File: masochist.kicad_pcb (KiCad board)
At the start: 2 copper layers, 195.3 x 103.2 mm, 76 parts, among them J1 USB_C_Receptacle_USB2.0, J2 AVR-ISP-6, SW1 RESET, SW2 SW_Push, U1 ATmega328P-PU, Y1 Crystal

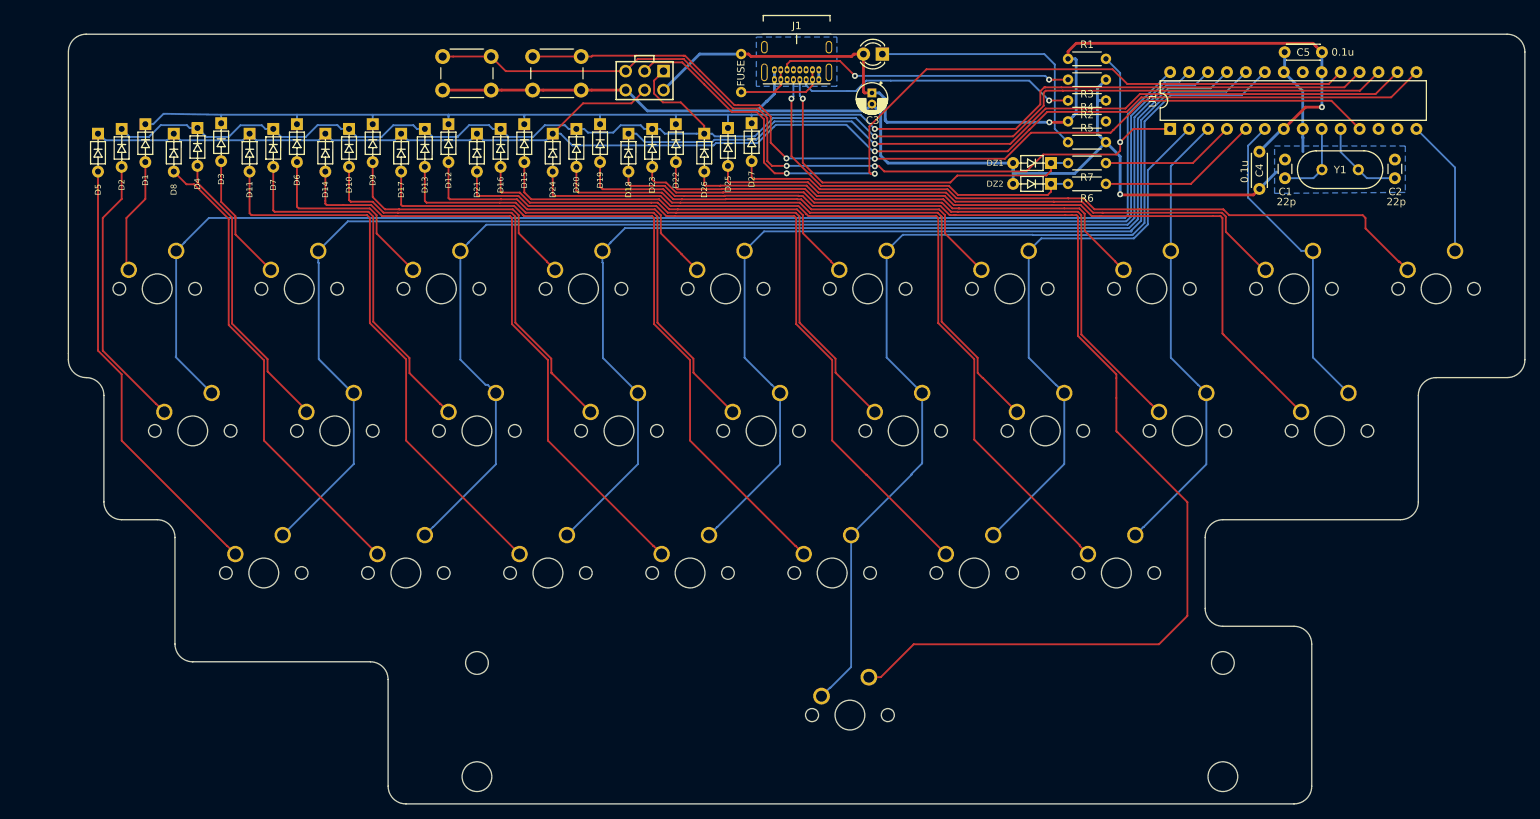
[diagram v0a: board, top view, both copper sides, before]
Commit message: added some mounting holes, waiting for feedback
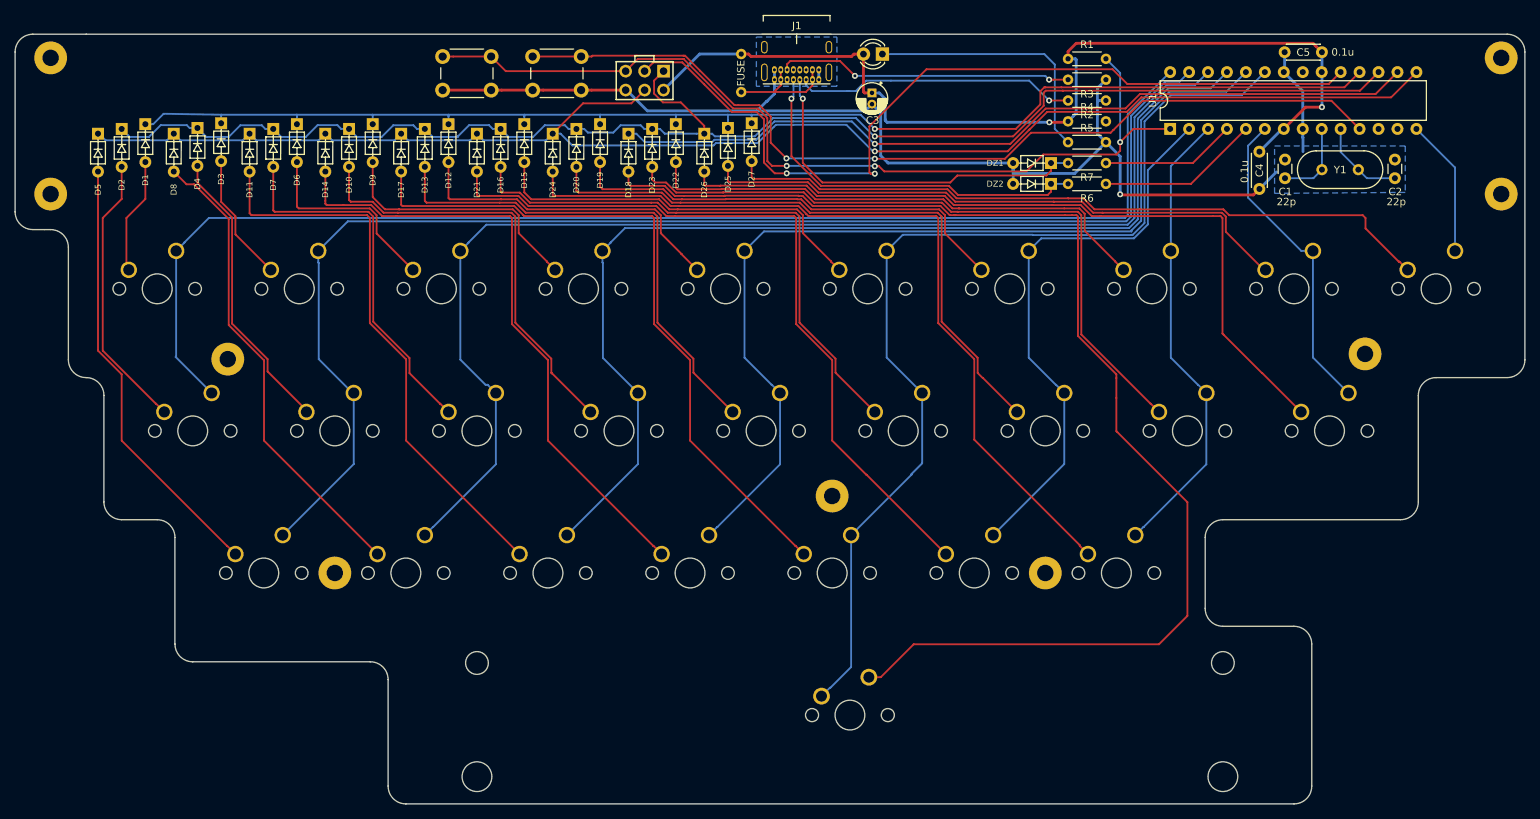
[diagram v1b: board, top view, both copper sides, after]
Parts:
- added REF**: MountingHole_2.2mm_M2_Pad, cftkb:MountingHole_2.2mm_M2_Pad, F.Cu at (63.5, 53.2)
- added REF**: MountingHole_2.2mm_M2_Pad, cftkb:MountingHole_2.2mm_M2_Pad, F.Cu at (63.5, 34.9)
- added REF**: MountingHole_2.2mm_M2_Pad, cftkb:MountingHole_2.2mm_M2_Pad, F.Cu at (258.0, 53.2)
- added REF**: MountingHole_2.2mm_M2_Pad, cftkb:MountingHole_2.2mm_M2_Pad, F.Cu at (258.0, 34.9)
- added REF**: MountingHole_2.2mm_M2_Pad, cftkb:MountingHole_2.2mm_M2_Pad, F.Cu at (168.3, 93.7)
- added REF**: MountingHole_2.2mm_M2_Pad, cftkb:MountingHole_2.2mm_M2_Pad, F.Cu at (239.7, 74.6)
- added REF**: MountingHole_2.2mm_M2_Pad, cftkb:MountingHole_2.2mm_M2_Pad, F.Cu at (196.8, 104.0)
- added REF**: MountingHole_2.2mm_M2_Pad, cftkb:MountingHole_2.2mm_M2_Pad, F.Cu at (101.6, 104.0)
- added REF**: MountingHole_2.2mm_M2_Pad, cftkb:MountingHole_2.2mm_M2_Pad, F.Cu at (87.2, 75.3)
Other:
- board size 195.3 x 103.2 mm -> 202.4 x 103.2 mm
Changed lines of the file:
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@@
   (general
     (thickness 1.6)
-    (drawings 32)
+    (drawings 37)
     (tracks 913)
     (zones 0)
-    (modules 76)
+    (modules 85)
     (nets 62)
   )
@@
     (add_net GND)
   )
+  (module cftkb:MountingHole_2.2mm_M2_Pad (layer F.Cu)
+    (at 63.5 53.18125)
+    (descr "Mounting Hole 2.2mm, M2")
+    (tags "mounting hole 2.2mm m2")
+    (attr virtual)
+    (fp_text reference REF** (at 0 -3.2) (layer Cmts.User)
+      (effects (font (size 1 1) (thickness 0.15)))
+    )
+    (fp_text value MountingHole_2.2mm_M2_Pad (at 0 3.2) (layer F.Fab)
+      (effects (font (size 1 1) (thickness 0.15)))
+    )
+    (fp_circle (center 0 0) (end 2.45 0) (layer F.CrtYd) (width 0.05))
+    (fp_circle (center 0 0) (end 2.2 0) (layer Cmts.User) (width 0.15))
+    (fp_text user %R (at 0.3 0) (layer F.Fab)
+      (effects (font (size 1 1) (thickness 0.15)))
+    )
+    (pad 1 thru_hole circle (at 0 0) (size 4.4 4.4) (drill 2.2) (layers *.Cu *.Mask))
+  )
+  (module cftkb:MountingHole_2.2mm_M2_Pad (layer F.Cu)
+    (at 63.5 34.925)
+    (descr "Mounting Hole 2.2mm, M2")
+    (tags "mounting hole 2.2mm m2")
+    (attr virtual)
+    (fp_text reference REF** (at 0 -3.2) (layer Cmts.User)
+      (effects (font (size 1 1) (thickness 0.15)))
+    )
+    (fp_text value MountingHole_2.2mm_M2_Pad (at 0 3.2) (layer F.Fab)
+      (effects (font (size 1 1) (thickness 0.15)))
+    )
+    (fp_circle (center 0 0) (end 2.45 0) (layer F.CrtYd) (width 0.05))
+    (fp_circle (center 0 0) (end 2.2 0) (layer Cmts.User) (width 0.15))
+    (fp_text user %R (at 0.3 0) (layer F.Fab)
+      (effects (font (size 1 1) (thickness 0.15)))
+    )
+    (pad 1 thru_hole circle (at 0 0) (size 4.4 4.4) (drill 2.2) (layers *.Cu *.Mask))
+  )
+  (module cftkb:MountingHole_2.2mm_M2_Pad (layer F.Cu)
+    (at 257.96875 53.18125)
+    (descr "Mounting Hole 2.2mm, M2")
+    (tags "mounting hole 2.2mm m2")
+    (attr virtual)
+    (fp_text reference REF** (at 0 -3.2) (layer Cmts.User)
+      (effects (font (size 1 1) (thickness 0.15)))
+    )
+    (fp_text value MountingHole_2.2mm_M2_Pad (at 0 3.2) (layer F.Fab)
+      (effects (font (size 1 1) (thickness 0.15)))
+    )
+    (fp_circle (center 0 0) (end 2.45 0) (layer F.CrtYd) (width 0.05))
+    (fp_circle (center 0 0) (end 2.2 0) (layer Cmts.User) (width 0.15))
+    (fp_text user %R (at 0.3 0) (layer F.Fab)
+      (effects (font (size 1 1) (thickness 0.15)))
+    )
+    (pad 1 thru_hole circle (at 0 0) (size 4.4 4.4) (drill 2.2) (layers *.Cu *.Mask))
+  )
+  (module cftkb:MountingHole_2.2mm_M2_Pad (layer F.Cu)
+    (at 257.96875 34.925)
+    (descr "Mounting Hole 2.2mm, M2")
+    (tags "mounting hole 2.2mm m2")
+    (attr virtual)
+    (fp_text reference REF** (at 0 -3.2) (layer Cmts.User)
+      (effects (font (size 1 1) (thickness 0.15)))
+    )
+    (fp_text value MountingHole_2.2mm_M2_Pad (at 0 3.2) (layer F.Fab)
+      (effects (font (size 1 1) (thickness 0.15)))
+    )
+    (fp_circle (center 0 0) (end 2.45 0) (layer F.CrtYd) (width 0.05))
+    (fp_circle (center 0 0) (end 2.2 0) (layer Cmts.User) (width 0.15))
+    (fp_text user %R (at 0.3 0) (layer F.Fab)
+      (effects (font (size 1 1) (thickness 0.15)))
+    )
+    (pad 1 thru_hole circle (at 0 0) (size 4.4 4.4) (drill 2.2) (layers *.Cu *.Mask))
+  )
+  (module cftkb:MountingHole_2.2mm_M2_Pad (layer F.Cu)
+    (at 168.275 93.6625)
+    (descr "Mounting Hole 2.2mm, M2")
+    (tags "mounting hole 2.2mm m2")
+    (attr virtual)
+    (fp_text reference REF** (at 0 -3.2) (layer Cmts.User)
+      (effects (font (size 1 1) (thickness 0.15)))
+    )
+    (fp_text value MountingHole_2.2mm_M2_Pad (at 0 3.2) (layer F.Fab)
+      (effects (font (size 1 1) (thickness 0.15)))
+    )
+    (fp_circle (center 0 0) (end 2.45 0) (layer F.CrtYd) (width 0.05))
+    (fp_circle (center 0 0) (end 2.2 0) (layer Cmts.User) (width 0.15))
+    (fp_text user %R (at 0.3 0) (layer F.Fab)
+      (effects (font (size 1 1) (thickness 0.15)))
+    )
+    (pad 1 thru_hole circle (at 0 0) (size 4.4 4.4) (drill 2.2) (layers *.Cu *.Mask))
+  )
+  (module cftkb:MountingHole_2.2mm_M2_Pad (layer F.Cu)
+    (at 239.7125 74.6125)
+    (descr "Mounting Hole 2.2mm, M2")
+    (tags "mounting hole 2.2mm m2")
+    (attr virtual)
+    (fp_text reference REF** (at 0 -3.2) (layer Cmts.User)
+      (effects (font (size 1 1) (thickness 0.15)))
+    )
+    (fp_text value MountingHole_2.2mm_M2_Pad (at 0 3.2) (layer F.Fab)
+      (effects (font (size 1 1) (thickness 0.15)))
+    )
+    (fp_circle (center 0 0) (end 2.45 0) (layer F.CrtYd) (width 0.05))
+    (fp_circle (center 0 0) (end 2.2 0) (layer Cmts.User) (width 0.15))
+    (fp_text user %R (at 0.3 0) (layer F.Fab)
+      (effects (font (size 1 1) (thickness 0.15)))
+    )
+    (pad 1 thru_hole circle (at 0 0) (size 4.4 4.4) (drill 2.2) (layers *.Cu *.Mask))
+  )
+  (module cftkb:MountingHole_2.2mm_M2_Pad (layer F.Cu)
+    (at 196.85 103.98125)
+    (descr "Mounting Hole 2.2mm, M2")
+    (tags "mounting hole 2.2mm m2")
+    (attr virtual)
+    (fp_text reference REF** (at 0 -3.2) (layer Cmts.User)
+      (effects (font (size 1 1) (thickness 0.15)))
+    )
+    (fp_text value MountingHole_2.2mm_M2_Pad (at 0 3.2) (layer F.Fab)
+      (effects (font (size 1 1) (thickness 0.15)))
+    )
+    (fp_circle (center 0 0) (end 2.45 0) (layer F.CrtYd) (width 0.05))
+    (fp_circle (center 0 0) (end 2.2 0) (layer Cmts.User) (width 0.15))
+    (fp_text user %R (at 0.3 0) (layer F.Fab)
+      (effects (font (size 1 1) (thickness 0.15)))
+    )
+    (pad 1 thru_hole circle (at 0 0) (size 4.4 4.4) (drill 2.2) (layers *.Cu *.Mask))
+  )
+  (module cftkb:MountingHole_2.2mm_M2_Pad (layer F.Cu)
+    (at 101.6 103.98125)
+    (descr "Mounting Hole 2.2mm, M2")
+    (tags "mounting hole 2.2mm m2")
+    (attr virtual)
+    (fp_text reference REF** (at 0 -3.2) (layer Cmts.User)
+      (effects (font (size 1 1) (thickness 0.15)))
+    )
+    (fp_text value MountingHole_2.2mm_M2_Pad (at 0 3.2) (layer F.Fab)
+      (effects (font (size 1 1) (thickness 0.15)))
+    )
+    (fp_circle (center 0 0) (end 2.45 0) (layer F.CrtYd) (width 0.05))
+    (fp_circle (center 0 0) (end 2.2 0) (layer Cmts.User) (width 0.15))
+    (fp_text user %R (at 0.3 0) (layer F.Fab)
+      (effects (font (size 1 1) (thickness 0.15)))
+    )
+    (pad 1 thru_hole circle (at 0 0) (size 4.4 4.4) (drill 2.2) (layers *.Cu *.Mask))
+  )
+  (module cftkb:MountingHole_2.2mm_M2_Pad (layer F.Cu)
+    (at 87.249 75.311)
+    (descr "Mounting Hole 2.2mm, M2")
+    (tags "mounting hole 2.2mm m2")
+    (attr virtual)
+    (fp_text reference REF** (at 0 -3.2) (layer Cmts.User)
+      (effects (font (size 1 1) (thickness 0.15)))
+    )
+    (fp_text value MountingHole_2.2mm_M2_Pad (at 0 3.2) (layer F.Fab)
+      (effects (font (size 1 1) (thickness 0.15)))
+    )
+    (fp_circle (center 0 0) (end 2.45 0) (layer F.CrtYd) (width 0.05))
+    (fp_circle (center 0 0) (end 2.2 0) (layer Cmts.User) (width 0.15))
+    (fp_text user %R (at 0.3 0) (layer F.Fab)
+      (effects (font (size 1 1) (thickness 0.15)))
+    )
+    (pad 1 thru_hole circle (at 0 0) (size 4.4 4.4) (drill 2.2) (layers *.Cu *.Mask))
+  )
   (module cftkb:Crystal_HC49-4H_Vertical (layer F.Cu)
     (at 233.934 49.911)
@@
     )
   )
+  (gr_line (start 62.70625 57.94375) (end 63.5 57.94375) (layer Edge.Cuts) (width 0.05))
+  (gr_line (start 61.11875 57.94375) (end 62.70625 57.94375) (layer Edge.Cuts) (width 0.05))
+  (gr_line (start 58.7375 34.13125) (end 58.7375 55.5625) (layer Edge.Cuts) (width 0.05))
+  (gr_arc (start 61.11875 55.5625) (end 58.7375 55.5625) (angle -90) (layer Edge.Cuts) (width 0.05))
+  (gr_line (start 65.88125 75.40625) (end 65.88125 60.325) (layer Edge.Cuts) (width 0.05))
+  (gr_arc (start 63.5 60.325) (end 65.88125 60.325) (angle -90) (layer Edge.Cuts) (width 0.05))
+  (gr_arc (start 68.2625 75.40625) (end 65.88125 75.40625) (angle -90) (layer Edge.Cuts) (width 0.05))
+  (gr_line (start 68.2625 31.75) (end 61.11875 31.75) (layer Edge.Cuts) (width 0.05))
+  (gr_arc (start 61.11875 34.13125) (end 61.11875 31.75) (angle -90) (layer Edge.Cuts) (width 0.05))
   (gr_line (start 261.14375 75.40625) (end 261.14375 34.13125) (layer Edge.Cuts) (width 0.05))
   (gr_line (start 249.2375 77.7875) (end 258.7625 77.7875) (layer Edge.Cuts) (width 0.05))
@@
   (gr_arc (start 73.025 94.45625) (end 70.64375 94.45625) (angle -90) (layer Edge.Cuts) (width 0.05))
   (gr_arc (start 68.2625 80.16875) (end 70.64375 80.16875) (angle -90) (layer Edge.Cuts) (width 0.05))
-  (gr_line (start 65.88125 74.6125) (end 65.88125 75.40625) (layer Edge.Cuts) (width 0.05))
-  (gr_arc (start 68.2625 75.40625) (end 65.88125 75.40625) (angle -90) (layer Edge.Cuts) (width 0.05))
-  (gr_line (start 65.88125 34.13125) (end 65.88125 74.6125) (layer Edge.Cuts) (width 0.05))
   (gr_line (start 258.7625 31.75) (end 68.2625 31.75) (layer Edge.Cuts) (width 0.05))
   (gr_arc (start 258.7625 34.13125) (end 261.14375 34.13125) (angle -90) (layer Edge.Cuts) (width 0.05))
-  (gr_arc (start 68.2625 34.13125) (end 68.2625 31.75) (angle -90) (layer Edge.Cuts) (width 0.05))
   (segment (start 228.82225 34.27475) (end 228.934 34.163) (width 0.25) (layer B.Cu) (net 1))
   (segment (start 231.36225 44.45) (end 231.394 44.45) (width 0.25) (layer F.Cu) (net 1))

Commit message: passes DRC, all traces connected
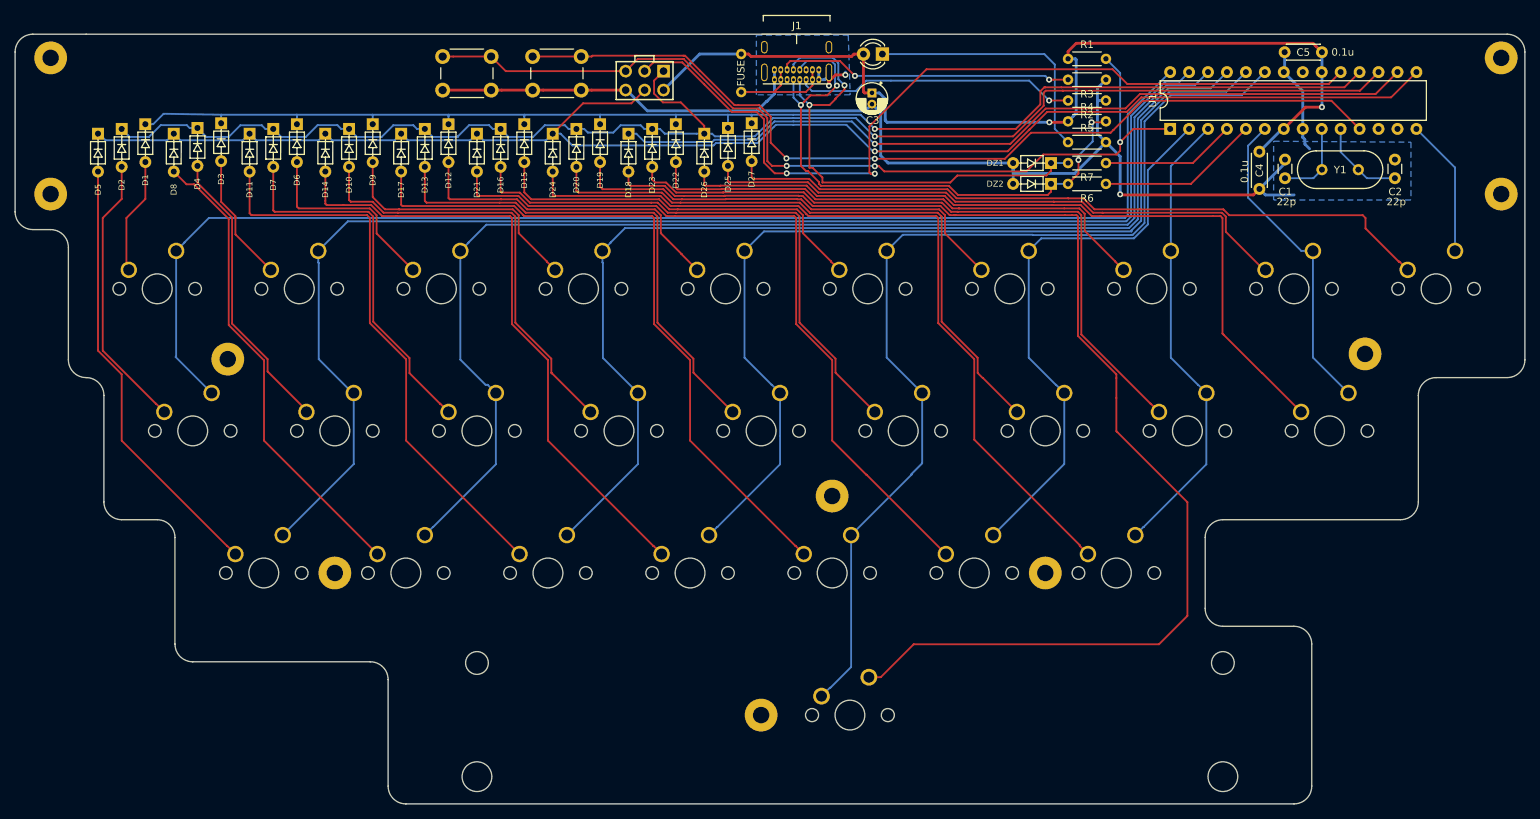
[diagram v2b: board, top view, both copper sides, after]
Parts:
- added REF**: MountingHole_2.2mm_M2_Pad, cftkb:MountingHole_2.2mm_M2_Pad, F.Cu at (158.8, 123.0)
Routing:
- net Net-(DZ2-Pad1): track 50.9 -> 77.0 mm, vias 1 -> 4
- net Net-(DZ1-Pad1): track 49.7 -> 66.9 mm, vias 1 -> 2
- net GND: track 166.5 -> 180.9 mm, vias 1 -> 3
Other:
- board text added: "Designed by Reid"
- board text added: "Masochist"

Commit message: added some cool dude's face to the silkscreen B)
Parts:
- added G***: LOGO, silkscreen:reid_face_tiny, B.Cu at (212.3, 120.9)

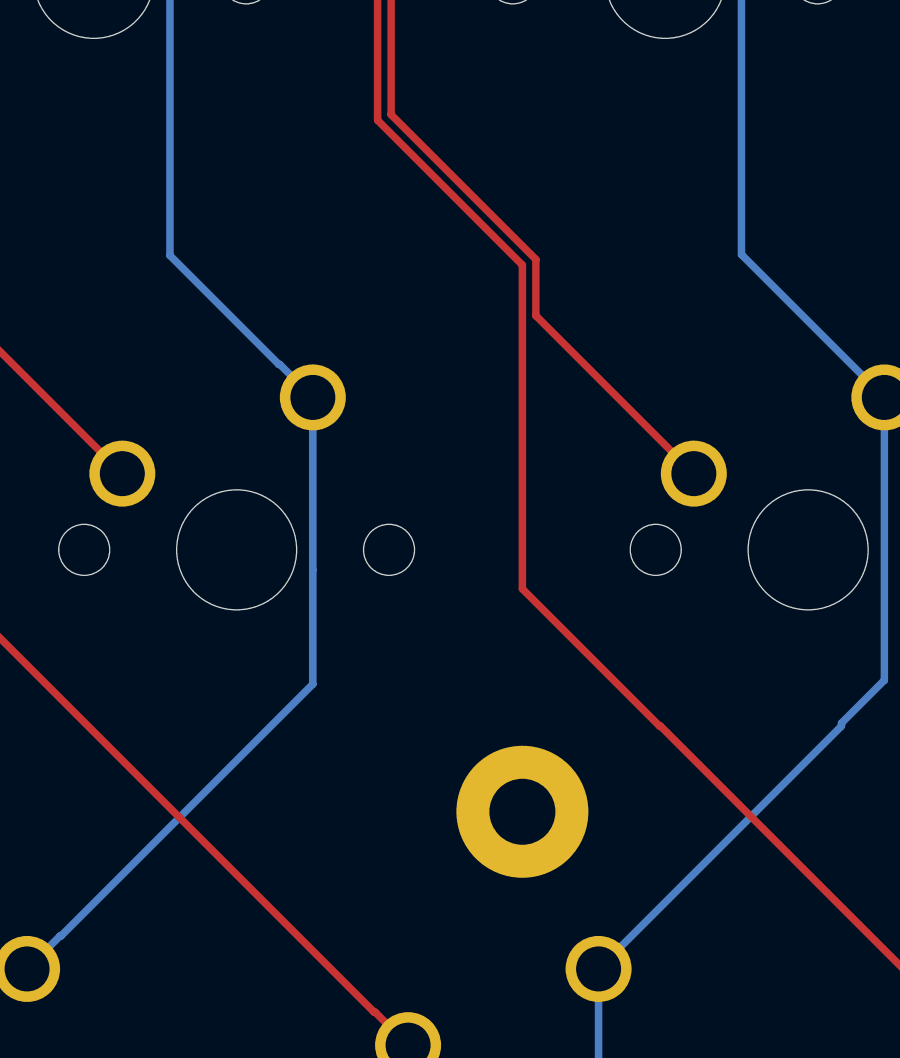
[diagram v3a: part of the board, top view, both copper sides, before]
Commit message: Added new logo silkscreen to PCB
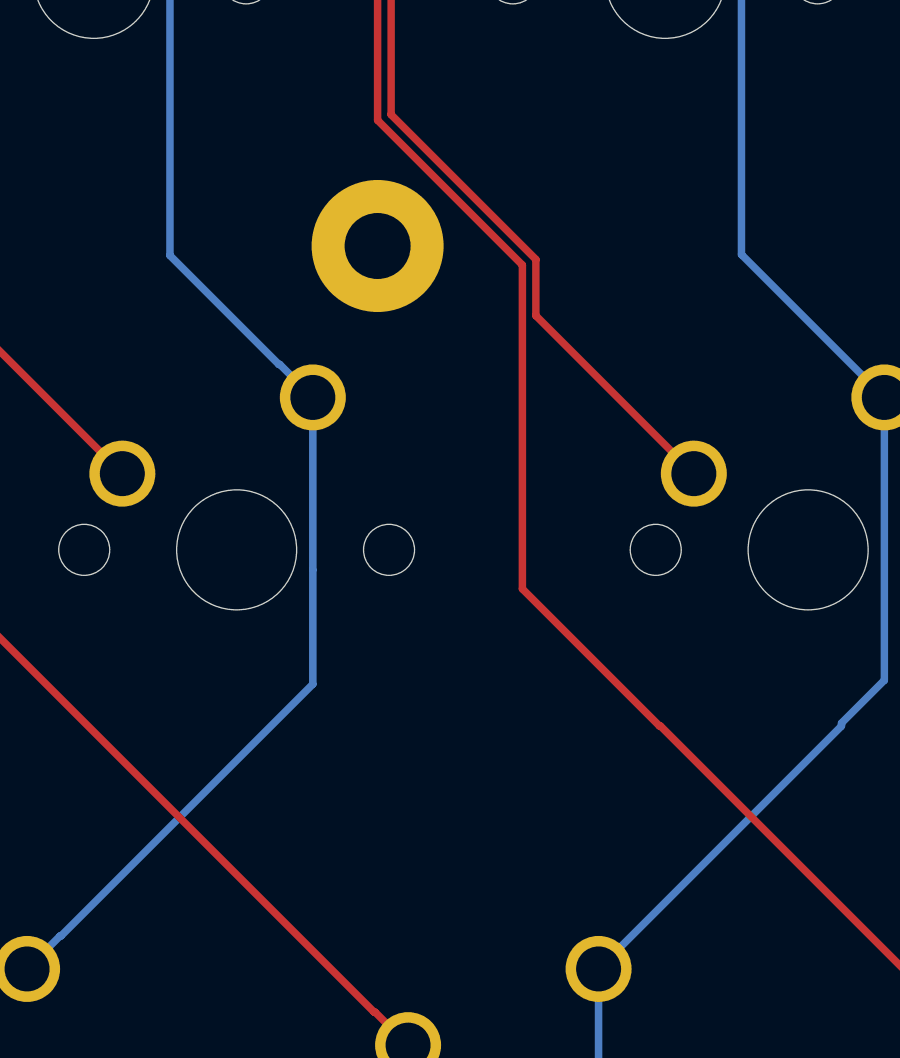
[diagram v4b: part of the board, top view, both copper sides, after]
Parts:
- removed the G*** at (212.3, 120.9)
- added G***: LOGO, silkscreen:masochist_script_logo, B.Cu at (202.6, 123.4)
- moved REF** 19.5 mm to (163.4, 74.8)
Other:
- board text added: "by Reid"
- board text removed: "Designed by Reid"
- board text removed: "Masochist"
